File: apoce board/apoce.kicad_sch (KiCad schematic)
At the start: 51 parts, among them J1 Test Soleil, J2 In-Sol, J3 Test J/N, J4 In-J/N, J5 Relais, J6 Screw_Terminal_01x02, SW1 ButModeJN, SW2 ButModeSolCAV, SW3 ButModeSolAuto, SW4 ButArmV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

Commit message: Etape 1 pour le placement routage
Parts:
- removed J2: In-Sol, symbol Connector:Conn_01x02_Pin
- removed J4: In-J/N, symbol Connector:Conn_01x02_Pin
- removed R16, R19, R21, R23, R25, R4, R6, R7, R8, R9: 220, symbol Device:R
- added J4: Jour/Nuit, TerminalBlock:TerminalBlock_bornier-2_P5.08mm, symbol Connector:Screw_Terminal_01x02
- D1: renamed from D2; footprint (none) -> LED_THT:LED_D5.0mm
- D10, D11, D12, D13, D3, D4, D5, D6, D7, D8, D9: footprint (none) -> LED_THT:LED_D5.0mm
- D2: renamed from D1; footprint (none) -> LED_THT:LED_D5.0mm
- J1, J3: footprint (none) -> TerminalBlock:TerminalBlock_Xinya_XY308-2.54-3P_1x03_P2.54mm_Horizontal
- J2: renamed from J6; value Screw_Terminal_01x02 -> Solaire; footprint Connector_Phoenix_MSTB:PhoenixContact_MSTBA_2,5_2-G_1x02_P5.00mm_Horizontal -> TerminalBlock_Phoenix:TerminalBlock_Phoenix_MKDS-1,5-2-5.08_1x02_P5.08mm_Horizontal
- J5: footprint (none) -> TerminalBlock:TerminalBlock_Xinya_XY308-2.54-6P_1x06_P2.54mm_Horizontal
- R1: footprint (none) -> Resistor_THT:R_Axial_DIN0207_L6.3mm_D2.5mm_P10.16mm_Horizontal
- R10: renamed from R18; footprint (none) -> Resistor_THT:R_Axial_DIN0207_L6.3mm_D2.5mm_P10.16mm_Horizontal
- R11: renamed from R20; footprint (none) -> Resistor_THT:R_Axial_DIN0207_L6.3mm_D2.5mm_P10.16mm_Horizontal
- R12: renamed from R22; footprint (none) -> Resistor_THT:R_Axial_DIN0207_L6.3mm_D2.5mm_P10.16mm_Horizontal
- R13: renamed from R24; footprint (none) -> Resistor_THT:R_Axial_DIN0207_L6.3mm_D2.5mm_P10.16mm_Horizontal
- R2: renamed from R3; value 270 -> 470; footprint (none) -> Resistor_THT:R_Axial_DIN0207_L6.3mm_D2.5mm_P10.16mm_Horizontal
- R3: renamed from R5; footprint (none) -> Resistor_THT:R_Axial_DIN0207_L6.3mm_D2.5mm_P10.16mm_Horizontal
- R4: renamed from R11; footprint (none) -> Resistor_THT:R_Axial_DIN0207_L6.3mm_D2.5mm_P10.16mm_Horizontal
- R5: renamed from R12; footprint (none) -> Resistor_THT:R_Axial_DIN0207_L6.3mm_D2.5mm_P10.16mm_Horizontal
- R6: renamed from R13; footprint (none) -> Resistor_THT:R_Axial_DIN0207_L6.3mm_D2.5mm_P10.16mm_Horizontal
- R7: renamed from R14; footprint (none) -> Resistor_THT:R_Axial_DIN0207_L6.3mm_D2.5mm_P10.16mm_Horizontal
- R8: renamed from R15; value 270 -> 470; footprint (none) -> Resistor_THT:R_Axial_DIN0207_L6.3mm_D2.5mm_P10.16mm_Horizontal
- R9: renamed from R17; footprint (none) -> Resistor_THT:R_Axial_DIN0207_L6.3mm_D2.5mm_P10.16mm_Horizontal
- SW1, SW2, SW3, SW4: footprint (none) -> TerminalBlock_Phoenix:TerminalBlock_Phoenix_MKDS-1,5-2-5.08_1x02_P5.08mm_Horizontal
- U1, U2: footprint Package_DIP:DIP-6_W7.62mm -> Package_DIP:DIP-6_W7.62mm_LongPads
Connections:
- net X: now also A1.20 (A1)
- net at R11.2: now also D11.2 (A)
- net at D7.1 (K): now also R7.1
- net at D6.1 (K): now also R6.1
- net at R12.2: now also D12.2 (A)
- net at R5.1: now also D5.1 (K)
- net at D3.2 (A): now also R2.2
- net at PS1.2 (AC/L): now also J2.2 (Pin_2)
- net at PS1.1 (AC/N): now also J2.1 (Pin_1)
- net at R8.2: now also D9.2 (A)
- net at PS2.2 (AC/L): now also J4.2 (Pin_2)
- net at PS2.1 (AC/N): now also J4.1 (Pin_1)
- net at R13.2: now also D13.2 (A)
- net at D4.1 (K): now also R4.1
- net at R10.2: now also D10.2 (A)
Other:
- moved on the sheet: D3, D9, J2, R4, R5, R6, R7

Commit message: Nouvelle version avec amélioration
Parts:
- D11: value LedModeSolCAV-Orange -> LedModeSol-Orange
- D12: value LedModeSolAuto-Rouge -> LedModeAuto-Rouge
- SW2: value ButModeSolCAV -> ButModeSol
- SW3: value ButModeSolAuto -> ButModeAuto
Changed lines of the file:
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@@
 			)
 		)
-		(property "Value" "ButModeSolCAV"
+		(property "Value" "ButModeSol"
 			(at 54.61 132.08 0)
 			(effects
@@
 			)
 		)
-		(property "Value" "LedModeSolCAV-Orange"
+		(property "Value" "LedModeSol-Orange"
 			(at 195.8975 129.54 0)
 			(effects
@@
 			)
 		)
-		(property "Value" "ButModeSolAuto"
+		(property "Value" "ButModeAuto"
 			(at 54.61 153.67 0)
 			(effects
@@
 			)
 		)
-		(property "Value" "LedModeSolAuto-Rouge"
+		(property "Value" "LedModeAuto-Rouge"
 			(at 195.8975 144.78 0)
 			(effects

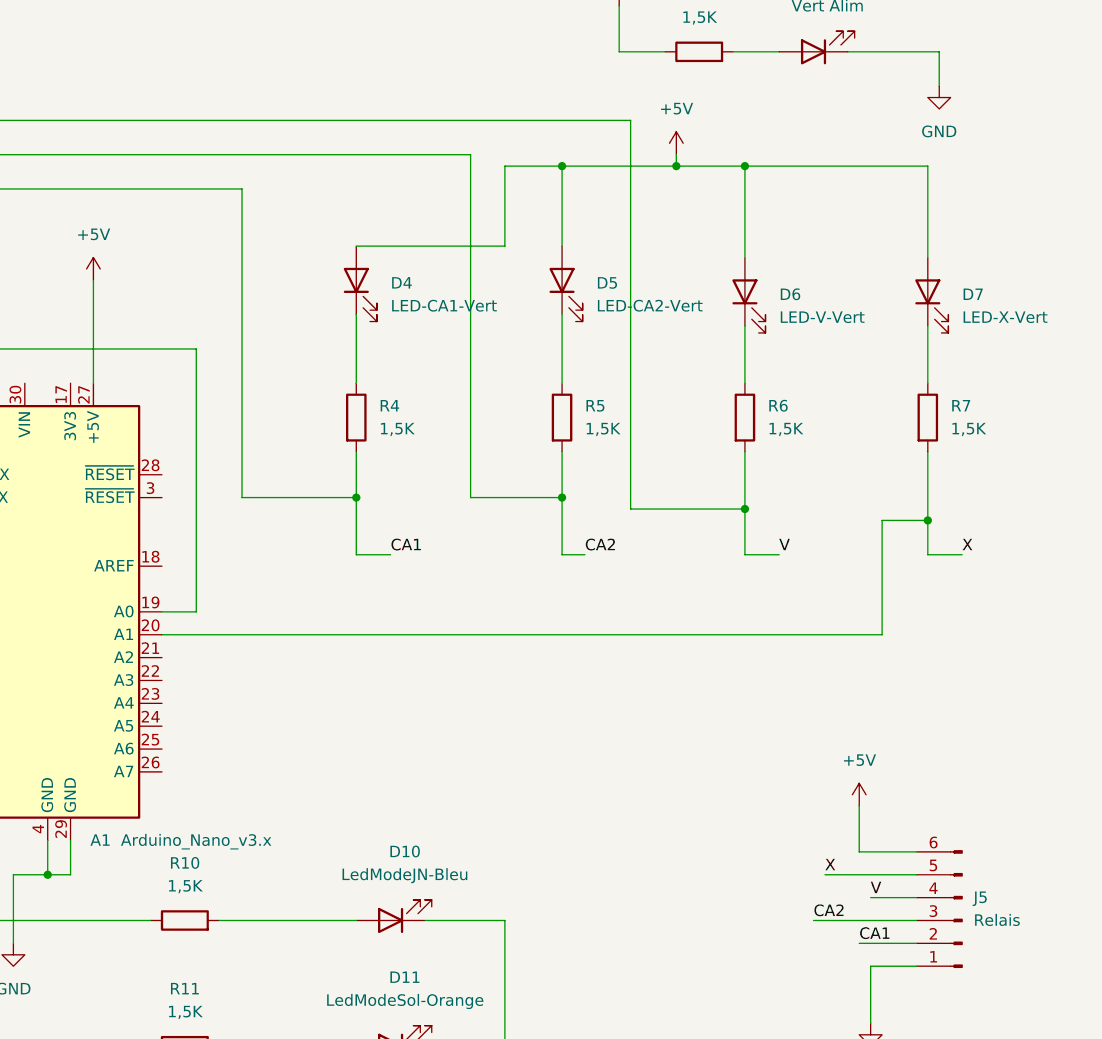
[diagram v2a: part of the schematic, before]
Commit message: On a séparer les compteurs  Led de forcage
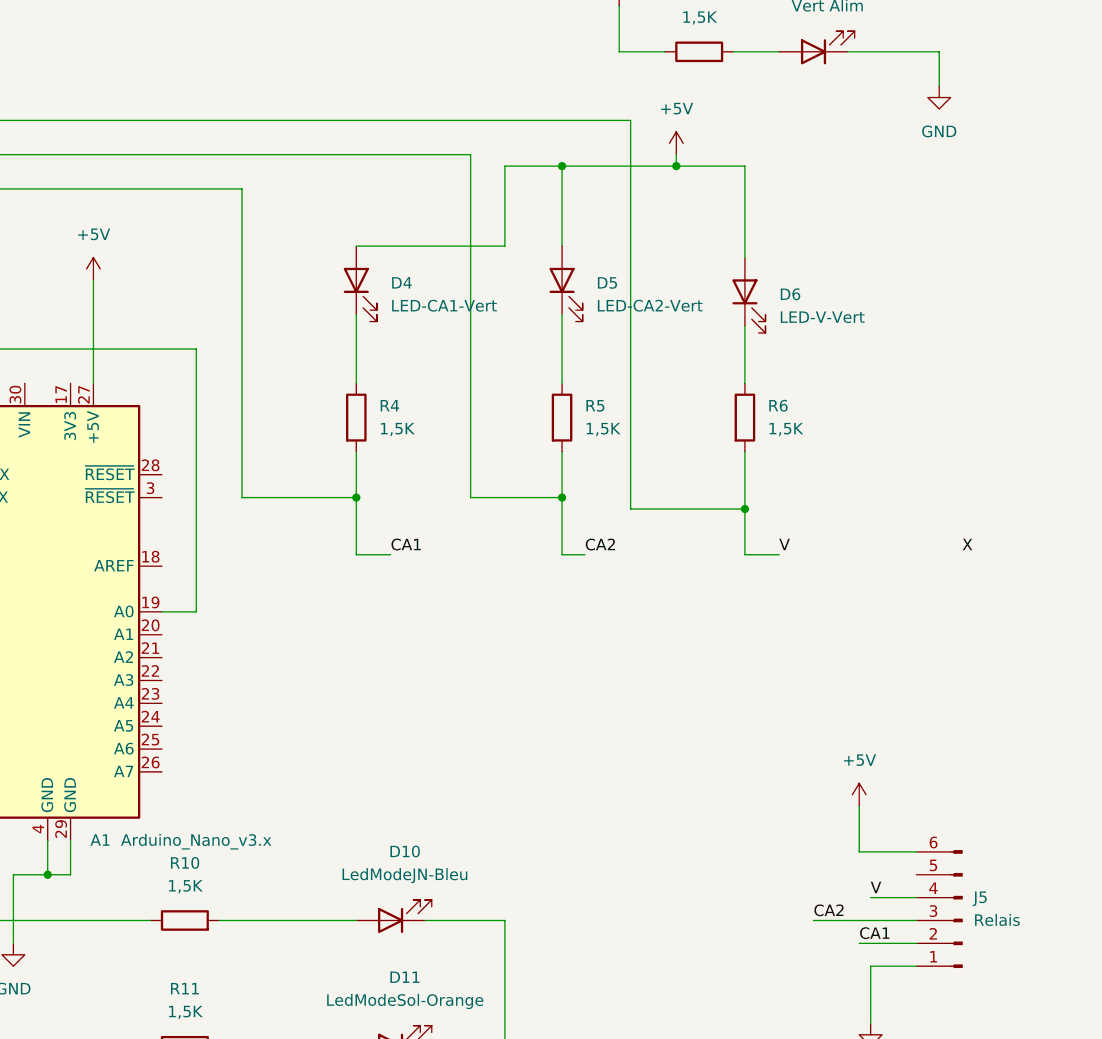
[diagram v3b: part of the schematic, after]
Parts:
- removed D7: LED-X-Vert, LED_THT:LED_D5.0mm, symbol Device:LED
- removed R7: 1,5K, Resistor_THT:R_Axial_DIN0207_L6.3mm_D2.5mm_P10.16mm_Horizontal, symbol Device:R
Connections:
- net X: no longer A1.20 (A1), J5.5 (Pin_5)
